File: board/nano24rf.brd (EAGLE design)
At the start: 17.4 x 50 mm, 18 parts

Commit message: added gerber for cestlation fike
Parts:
- JP1, JP2: device microbuilder:1X15_ROUND_70 -> nano24rf:1X15_LONG
- moved MOSFET-12 0.64 mm to (1.91, 5.08)
- moved MOSFET-34 0.51 mm to (16.0, 5.08)
- flipped JP1 to the bottom
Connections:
- net 3V3: now also JP1.P$2; no longer JP1.2
- net CE: now also JP2.P$6; no longer JP2.6
- net CSN: now also JP2.P$5; no longer JP2.5
- net D10: now also JP2.P$3; no longer JP2.3
- net D5: now also JP2.P$8; no longer JP2.8
- net D6: now also JP2.P$7; no longer JP2.7
- net D9: now also JP2.P$4; no longer JP2.4
- net GND: now also JP1.P$14, JP1.P$3, JP2.P$12; no longer JP1.14, JP1.3, JP2.12
- net SCL: now also JP1.P$9; no longer JP1.9
- net SDA: now also JP1.P$8; no longer JP1.8
- net VIN: now also JP1.P$15; no longer JP1.15
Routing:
- net GND: track 26.3 -> 10.3 mm, vias 2 -> 1
- net FET04: track 48.1 -> 55.6 mm
- net FET02: track 21.1 -> 24.2 mm, vias 0 -> 2
- net 3V3: track 57.6 -> 59.3 mm, vias 1 -> 2
- net VIN: track 18.4 -> 17.5 mm
- net CSK: track 18.7 -> 18.2 mm
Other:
- board size 17.4 x 50 mm -> 15.3 x 50 mm

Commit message: back to round ads
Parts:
- JP1, JP2: device nano24rf:1X15_LONG -> nano24rf:1X15_ROUND_70
- moved MOSFET-34 1.78 mm to (17.8, 5.16)
- moved MOSFET-12 1.09 mm to (0.81, 5.03)
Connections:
- net 3V3: now also JP1.2; no longer JP1.P$2
- net CE: now also JP2.6; no longer JP2.P$6
- net CSN: now also JP2.5; no longer JP2.P$5
- net D10: now also JP2.3; no longer JP2.P$3
- net D5: now also JP2.8; no longer JP2.P$8
- net D6: now also JP2.7; no longer JP2.P$7
- net D9: now also JP2.4; no longer JP2.P$4
- net GND: now also JP1.14, JP1.3, JP2.12; no longer JP1.P$14, JP1.P$3, JP2.P$12
- net SCL: now also JP1.9; no longer JP1.P$9
- net SDA: now also JP1.8; no longer JP1.P$8
- net VIN: now also JP1.15; no longer JP1.P$15
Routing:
- net VIN: track 17.5 -> 20.2 mm
- net FET03: track 59.5 -> 60.7 mm
- net FET01: track 30.0 -> 31.1 mm
- net FET02: track 24.2 -> 25.2 mm
- net FET04: track 55.6 -> 56.6 mm
- net CE: track 34.3 -> 33.8 mm
- net D5: track 16.3 -> 15.8 mm
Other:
- board size 15.3 x 50 mm -> 17.8 x 49.5 mm

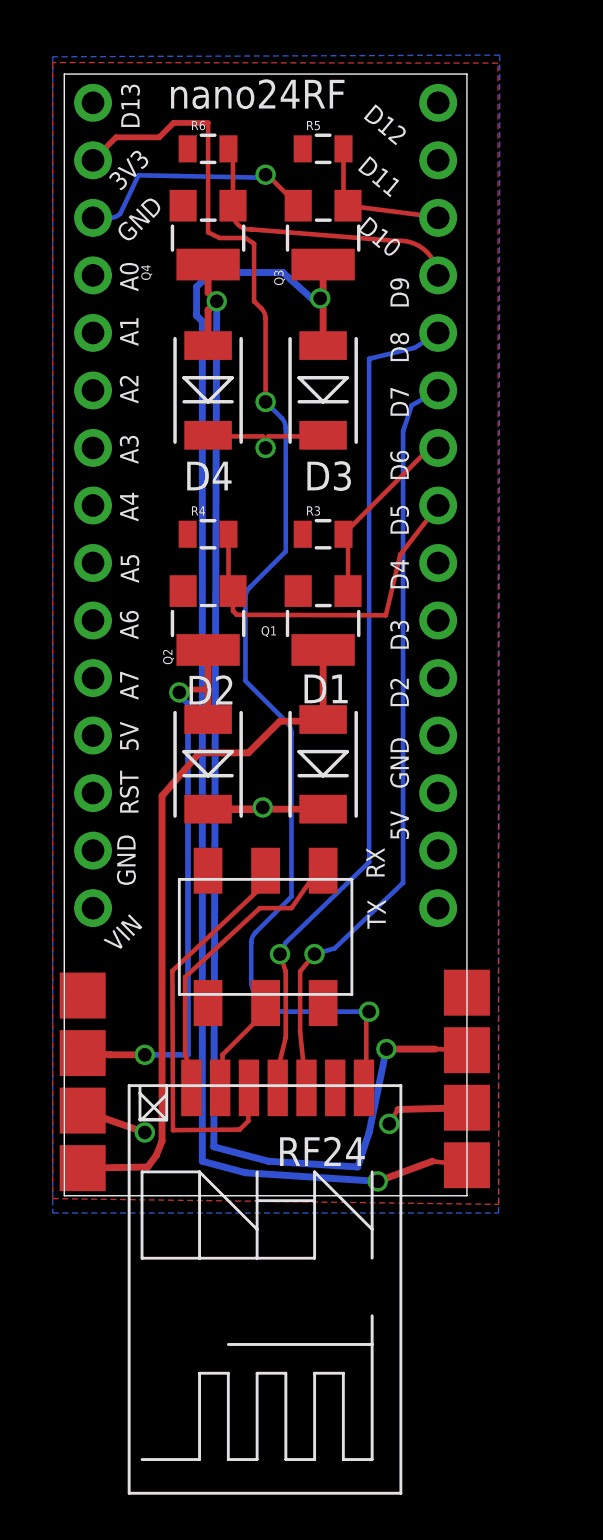
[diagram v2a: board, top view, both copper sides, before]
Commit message: long pads
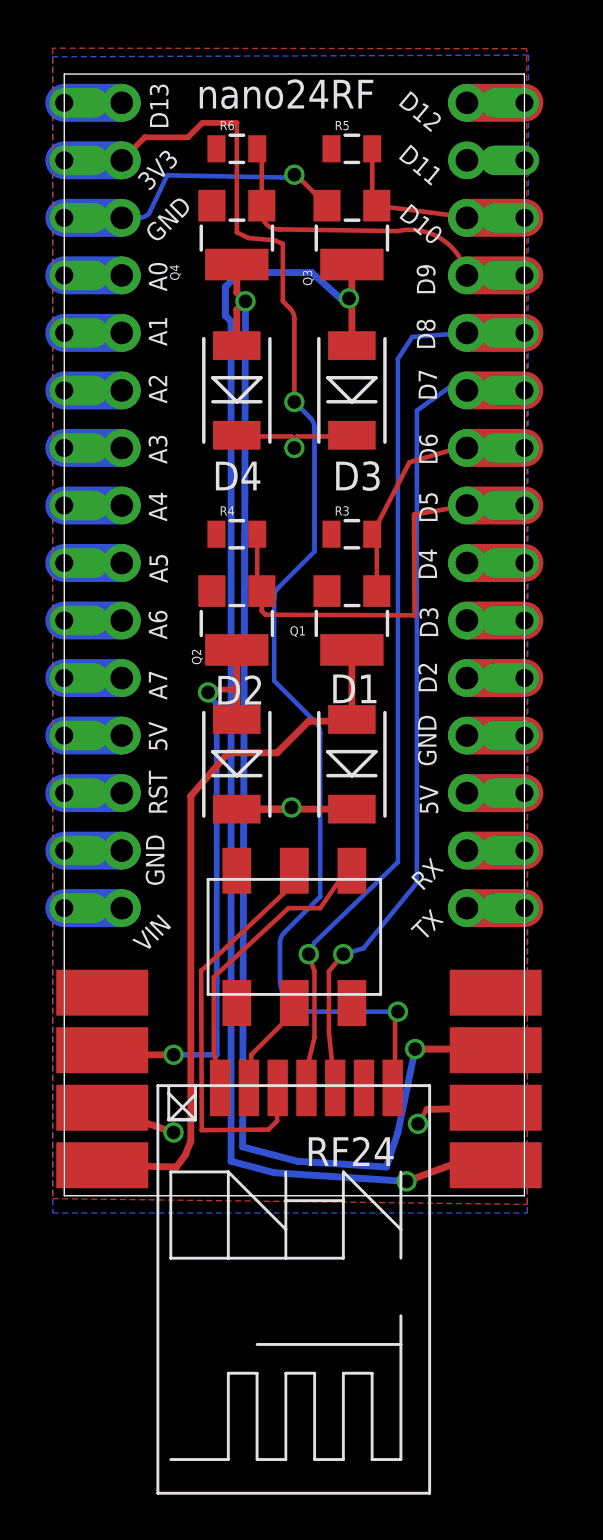
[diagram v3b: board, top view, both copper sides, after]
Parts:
- added JP4, JP5: (no value), nano24rf:1X15_LONG
- MOSFET-12, MOSFET-34: value FATPAD4 -> FATPAD4LONG; device nano24rf:FATPAD4 -> nano24rf:FATFAD4-LONG
- moved D2 1.27 mm to (7.62, 19.1)
- moved D4 1.27 mm to (7.62, 35.6)
- moved Q2 1.27 mm to (7.62, 25.4)
- moved Q4 1.27 mm to (7.62, 42.4)
- moved R4 1.27 mm to (7.62, 29.2)
- moved R6 1.27 mm to (7.62, 46.2)
- moved JP1 1.27 mm to (2.54, 30.5)
- moved RF24 1.27 mm to (4.06, 4.95)
- moved D1 1.27 mm to (12.7, 19.1)
- moved D3 1.27 mm to (12.7, 35.6)
- moved JP2 1.27 mm to (17.8, 30.5)
- moved JP3 1.27 mm to (10.2, 11.4)
- moved MOSFET-34 1.27 mm to (19.1, 5.16)
- moved Q1 1.27 mm to (12.7, 25.4)
- moved Q3 1.27 mm to (12.7, 42.4)
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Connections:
- new net N$10: JP1.11, JP4.P$11
- new net N$11: JP1.12, JP4.P$12
- new net N$12: JP1.13, JP4.P$13
- new net N$13: JP2.15, JP5.P$15
- new net N$14: JP2.14, JP5.P$14
- new net N$15: JP2.13, JP5.P$13
- new net N$16: JP2.11, JP5.P$11
- new net N$17: JP2.10, JP5.P$10
- new net N$18: JP2.9, JP5.P$9
- new net N$19: JP2.2, JP5.P$2
- new net N$20: JP2.1, JP5.P$1
- new net N$4: JP1.1, JP4.P$1
- new net N$5: JP1.4, JP4.P$4
- new net N$6: JP1.5, JP4.P$5
- new net N$7: JP1.6, JP4.P$6
- new net N$8: JP1.7, JP4.P$7
- new net N$9: JP1.10, JP4.P$10
- net 3V3: now also JP4.P$2
- net CE: now also JP5.P$6
- net CSN: now also JP5.P$5
- net D10: now also JP5.P$3
- net D5: now also JP5.P$8
- net D6: now also JP5.P$7
- net D9: now also JP5.P$4
- net GND: now also JP4.P$14, JP4.P$3, JP5.P$12
- net SCL: now also JP4.P$9
- net SDA: now also JP4.P$8
- net VIN: now also JP4.P$15
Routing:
- net GND: track 10.7 -> 18.4 mm
- net D5: track 15.8 -> 19.6 mm
- net CE: track 33.8 -> 36.8 mm
- net D6: track 8.35 -> 11.3 mm
- net VIN: track 20.2 -> 23.2 mm
- net CSN: track 37.3 -> 40.1 mm
- net D9: track 12.8 -> 15.4 mm
- net SDA: track 0.00 -> 2.54 mm
- net SCL: track 0.00 -> 2.54 mm
- net N$9: track 0.00 -> 2.54 mm
- net N$8: track 0.00 -> 2.54 mm
- net N$7: track 0.00 -> 2.54 mm
- net N$6: track 0.00 -> 2.54 mm
- net N$5: track 0.00 -> 2.54 mm
- net N$4: track 0.00 -> 2.54 mm
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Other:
- board size 17.8 x 49.5 mm -> 20.3 x 49.5 mm

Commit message: slight schema re-arange, and gerber
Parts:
- moved MOSFET-12 0.26 mm to (1.45, 5.03)
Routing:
- net N$19: track 0.00 -> 2.54 mm

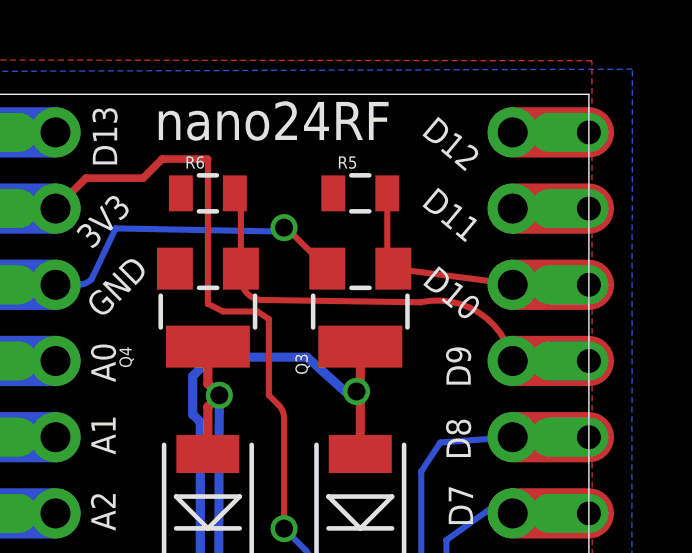
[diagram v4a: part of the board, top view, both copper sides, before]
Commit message: switched to pin11 one of the mosfet
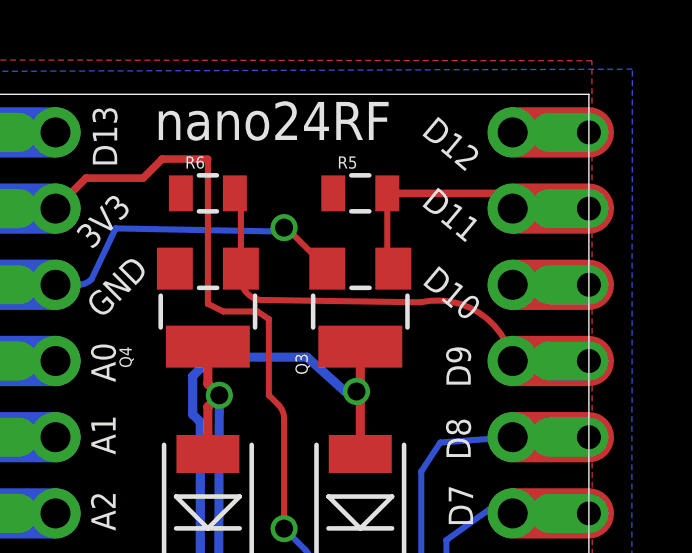
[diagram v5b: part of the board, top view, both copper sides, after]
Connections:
- removed net N$19: JP2.2, JP5.P$2
- new net D11: JP2.2, JP5.P$2, Q3.1, R5.2
- net D10: no longer Q3.1, R5.2
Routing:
- net D11: track 0.00 -> 9.52 mm
- net D10: track 9.16 -> 2.58 mm
- net N$19: track 2.54 -> 0.00 mm
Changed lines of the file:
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@@
 <signal name="D10">
 <contactref element="JP2" pad="3"/>
-<contactref element="Q3" pad="1"/>
-<contactref element="R5" pad="2"/>
-<wire x1="13.6" y1="46.228" x2="13.6" y2="43.918" width="0.2032" layer="1"/>
-<wire x1="13.6" y1="43.918" x2="13.8" y2="43.718" width="0.2032" layer="1" curve="90"/>
-<wire x1="13.8" y1="43.718" x2="17.75" y2="43.21" width="0.2032" layer="1"/>
 <wire x1="17.75" y1="43.21" x2="17.78" y2="43.18" width="0.2032" layer="1" curve="-90"/>
 <contactref element="JP5" pad="P$3"/>
@@
 <wire x1="17.78" y1="27.94" x2="20.32" y2="27.94" width="1.6764" layer="1"/>
 </signal>
-<signal name="N$19">
-<contactref element="JP2" pad="2"/>
-<contactref element="JP5" pad="P$2"/>
-<wire x1="17.78" y1="45.72" x2="20.32" y2="45.72" width="1.6764" layer="1"/>
-</signal>
 <signal name="N$20">
 <contactref element="JP5" pad="P$1"/>
@@
 <wire x1="17.78" y1="48.26" x2="20.32" y2="48.26" width="1.6764" layer="1"/>
 </signal>
+<signal name="D11">
+<contactref element="JP2" pad="2"/>
+<contactref element="JP5" pad="P$2"/>
+<wire x1="17.78" y1="45.72" x2="20.32" y2="45.72" width="1.6764" layer="1"/>
+<contactref element="Q3" pad="1"/>
+<contactref element="R5" pad="2"/>
+<wire x1="13.6" y1="46.228" x2="13.6" y2="43.918" width="0.2032" layer="1"/>
+<wire x1="13.6" y1="43.918" x2="13.8" y2="43.718" width="0.2032" layer="1" curve="90"/>
+<wire x1="13.6" y1="46.228" x2="17.272" y2="46.228" width="0.254" layer="1"/>
+<wire x1="17.272" y1="46.228" x2="17.78" y2="45.72" width="0.254" layer="1" curve="-90"/>
+</signal>
 </signals>

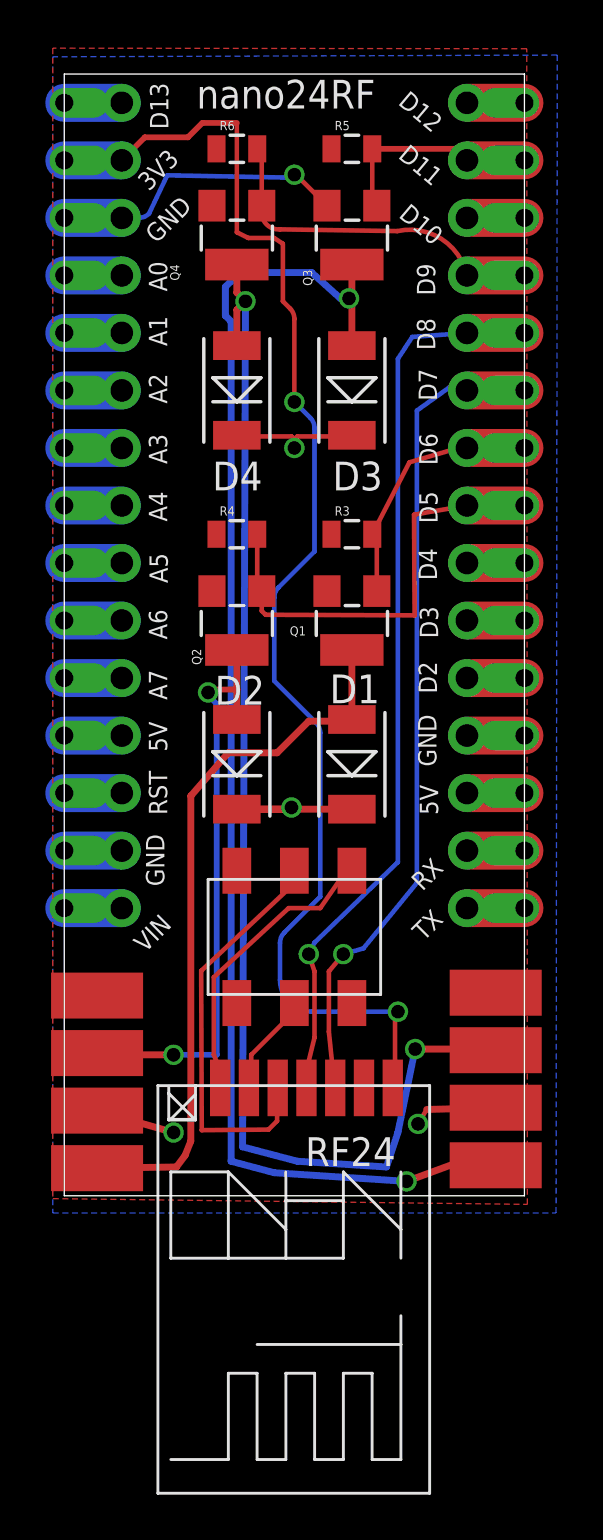
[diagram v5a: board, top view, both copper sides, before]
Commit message: removed SPI
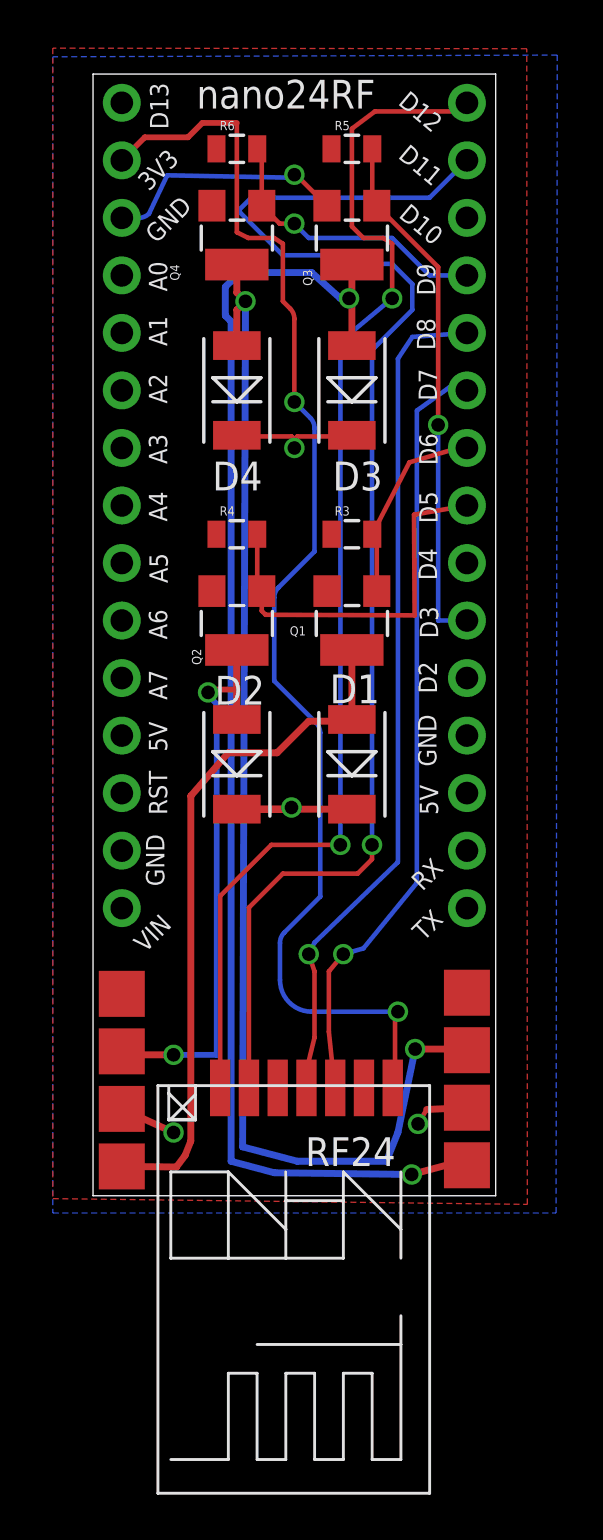
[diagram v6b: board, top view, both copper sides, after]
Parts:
- removed JP3: (no value), nano24rf:2X03_SMT
- removed JP4, JP5: (no value), nano24rf:1X15_LONG
- MOSFET-12, MOSFET-34: value FATPAD4LONG -> FATPAD4SEQ; device nano24rf:FATFAD4-LONG -> nano24rf:FATPAD4
- moved MOSFET-34 1.27 mm to (17.8, 5.16)
- moved MOSFET-12 1.09 mm to (2.54, 5.11)
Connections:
- removed net 5V: JP3.2
- removed net D10: JP2.3, JP5.P$3
- removed net D11: JP2.2, JP5.P$2, Q3.1, R5.2
- removed net N$10: JP1.11, JP4.P$11
- removed net N$11: JP1.12, JP4.P$12
- removed net N$12: JP1.13, JP4.P$13
- removed net N$13: JP2.15, JP5.P$15
- removed net N$14: JP2.14, JP5.P$14
- removed net N$15: JP2.13, JP5.P$13
- removed net N$16: JP2.11, JP5.P$11
- removed net N$17: JP2.10, JP5.P$10
- removed net N$18: JP2.9, JP5.P$9
- removed net N$20: JP2.1, JP5.P$1
- removed net N$4: JP1.1, JP4.P$1
- removed net N$5: JP1.4, JP4.P$4
- removed net N$6: JP1.5, JP4.P$5
- removed net N$7: JP1.6, JP4.P$6
- removed net N$8: JP1.7, JP4.P$7
- removed net N$9: JP1.10, JP4.P$10
- removed net RST: JP3.5
- new net D3: JP2.10, Q3.1, R5.2
- new net SCK: JP1.1
- net 3V3: no longer JP4.P$2
- net CE: no longer JP5.P$6
- net CSK: no longer JP3.3
- net CSN: no longer JP5.P$5
- net D5: no longer JP5.P$8
- net D6: no longer JP5.P$7
- net D9: no longer JP5.P$4
- net GND: no longer JP3.6, JP4.P$14, JP4.P$3, JP5.P$12
- net MISO: now also JP2.1; no longer JP3.1
- net MOSI: now also JP2.2; no longer JP3.4
- net SCL: no longer JP4.P$9
- net SDA: no longer JP4.P$8
- net VIN: no longer JP4.P$15
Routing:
- net MOSI: track 4.58 -> 60.4 mm, vias 0 -> 1
- net MISO: track 13.1 -> 54.2 mm, vias 0 -> 2
- net D3: track 0.00 -> 23.3 mm, vias 0 -> 1
- net CSK: track 18.2 -> 0.00 mm
- net D11: track 9.52 -> 0.00 mm
- net GND: track 18.4 -> 10.7 mm
- net VIN: track 23.4 -> 18.5 mm
- net D10: track 2.58 -> 0.00 mm
- net SDA: track 2.54 -> 0.00 mm
- net SCL: track 2.54 -> 0.00 mm
- net N$9: track 2.54 -> 0.00 mm
- net N$8: track 2.54 -> 0.00 mm
- net N$7: track 2.54 -> 0.00 mm
- net N$6: track 2.54 -> 0.00 mm
- net N$5: track 2.54 -> 0.00 mm
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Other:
- board size 20.3 x 49.5 mm -> 17.8 x 49.5 mm

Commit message: re-routed D10 to MOSFET
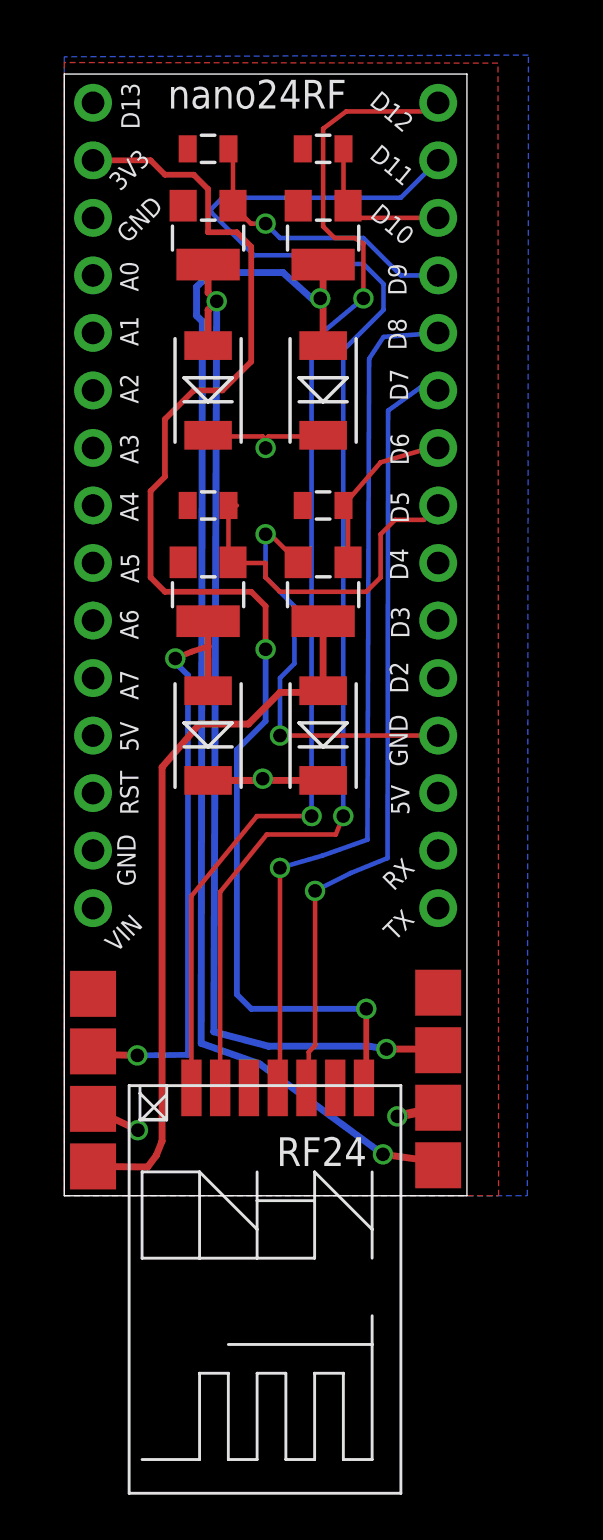
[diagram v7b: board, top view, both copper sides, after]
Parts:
- moved Q2 1.80 mm to (6.35, 26.7)
- moved Q1 1.80 mm to (11.4, 26.7)
- moved D2 1.80 mm to (6.35, 20.3)
- moved R4 1.80 mm to (6.35, 30.5)
- moved D1 1.80 mm to (11.4, 20.3)
- moved R3 1.80 mm to (11.4, 30.5)
- moved D4 1.27 mm to (6.35, 35.6)
- moved Q4 1.27 mm to (6.35, 42.4)
- moved R6 1.27 mm to (6.35, 46.2)
- moved JP1 1.27 mm to (1.27, 30.5)
- moved MOSFET-12 1.27 mm to (1.27, 5.11)
- moved RF24 1.27 mm to (2.79, 4.95)
- moved D3 1.27 mm to (11.4, 35.6)
- moved JP2 1.27 mm to (16.5, 30.5)
- moved MOSFET-34 1.27 mm to (16.5, 5.16)
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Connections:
- removed net D3: JP2.10, Q3.1, R5.2
- new net D10: JP2.3, Q3.1, R5.2
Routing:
- net D3: track 23.3 -> 0.00 mm, vias 1 -> 0
- net FET04: track 55.1 -> 46.2 mm
- net GND: track 10.7 -> 18.6 mm, vias 1 -> 2
- net D10: track 0.00 -> 6.80 mm
- net FET03: track 59.4 -> 55.6 mm
- net FET02: track 24.8 -> 26.5 mm
- net D5: track 17.1 -> 15.6 mm
- net 3V3: track 59.3 -> 60.6 mm
- net CSN: track 37.6 -> 38.8 mm
- net FET01: track 30.6 -> 31.9 mm
- net D6: track 8.80 -> 7.74 mm
- net VIN: track 18.5 -> 17.5 mm
- net MISO: track 54.2 -> 53.7 mm
